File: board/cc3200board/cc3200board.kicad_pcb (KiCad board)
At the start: 4 copper layers, 40.4 x 30.8 mm, 44 parts, among them P1 PROG, P3 CONN_JTAG, U1 CC3200R1M2RGCR, U2 N25Q128A13ESE40E, X1 32.768kH, X2 ABM3B-40.000MHZ-10-1-U-T

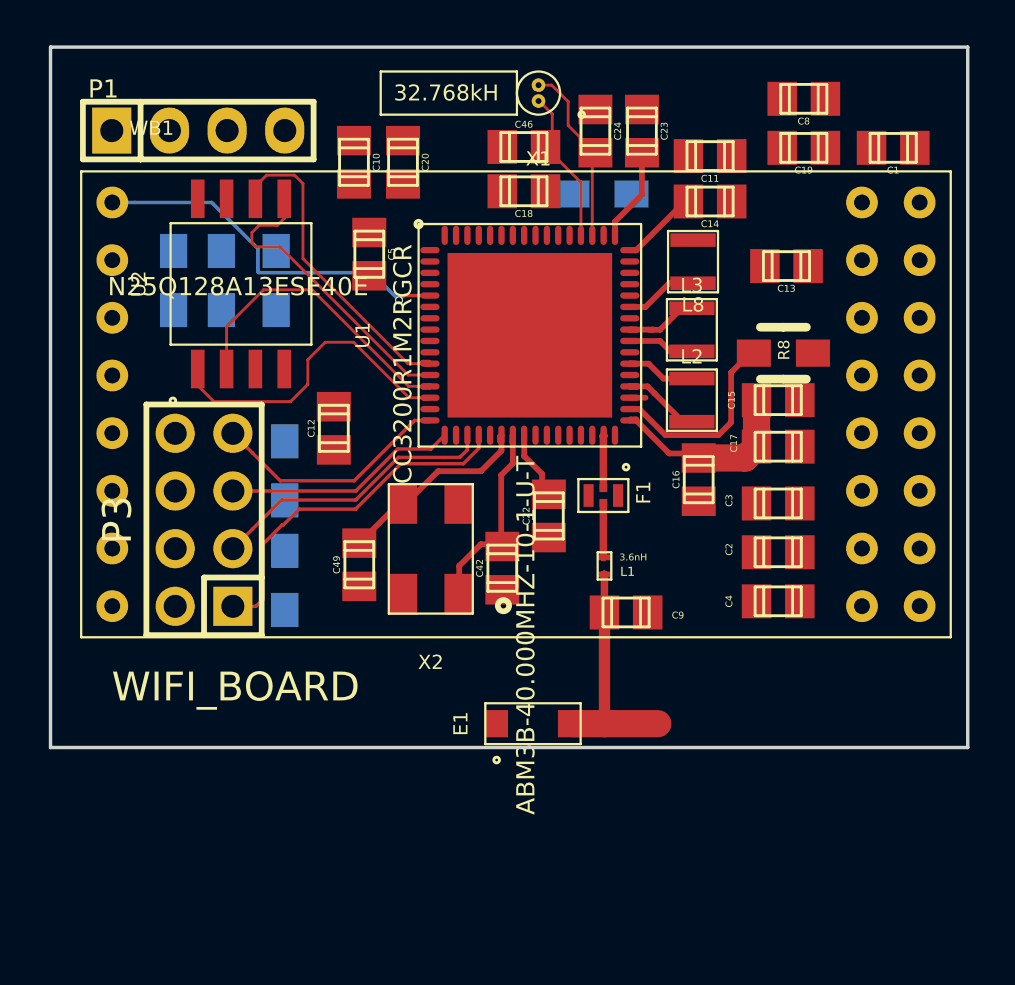
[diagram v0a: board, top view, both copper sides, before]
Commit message: Routed PA and DIG power planes
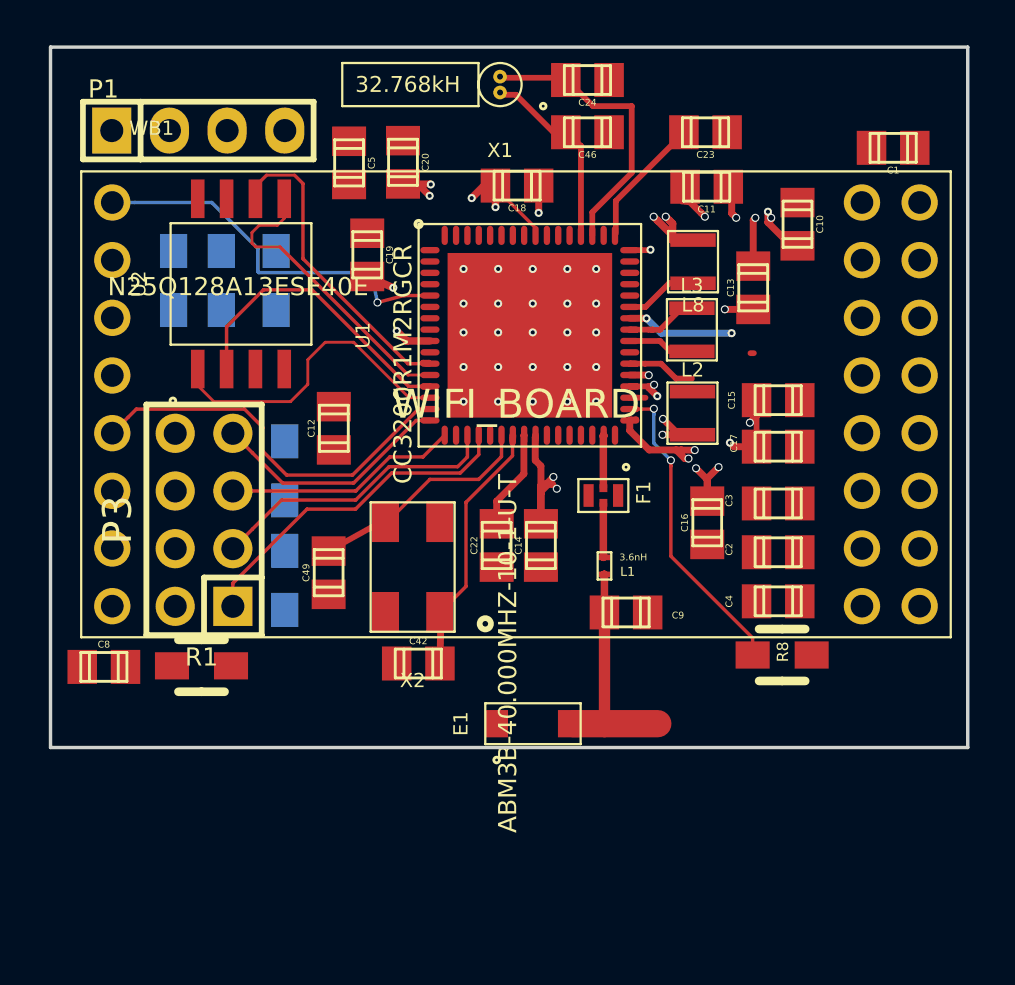
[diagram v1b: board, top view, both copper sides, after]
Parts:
- R1: moved to F.Cu
- moved C8 39.7 mm to (117.0, 155.4), turned to 0 degrees
- moved R1 27.3 mm to (121.3, 155.4)
- moved C19 19.8 mm to (128.6, 137.3), turned to 270 degrees
- moved C10 19.7 mm to (147.6, 135.9)
- moved C14 16.9 mm to (136.2, 150.1), turned to 90 degrees
- moved R8 13.3 mm to (146.9, 154.9)
- moved C42 5.60 mm to (130.8, 155.3), turned to 0 degrees
- moved C5 4.12 mm to (127.8, 133.2)
- moved C46 2.87 mm to (138.3, 131.9), turned to 180 degrees
- moved C23 2.80 mm to (143.5, 131.9), turned to 180 degrees
- moved C22 2.64 mm to (134.3, 150.1)
- moved C24 2.28 mm to (138.3, 129.6), turned to 180 degrees
- moved C16 1.94 mm to (143.6, 149.1)
- moved C13 1.75 mm to (145.6, 138.8), turned to 90 degrees
- moved X1 1.74 mm to (134.4, 129.8)
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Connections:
- net Net-(C10-Pad1) renamed /DCDC_ANA
- net Net-(C15-Pad1) renamed /DC_PA
- net Net-(C18-Pad1) renamed /DCDC_DIG
- U1 pad 26: (no net) -> Net-(U1-Pad26)
- U1 pad 27: (no net) -> Net-(U1-Pad27)
- U1 pad 28: (no net) -> Net-(U1-Pad28)
- U1 pad 29: (no net) -> Net-(U1-Pad29)
- U1 pad 30: (no net) -> Net-(U1-Pad30)
- U1 pad 46: (no net) -> Net-(U1-Pad46)
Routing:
- net GND: track 10.4 -> 68.9 mm, vias 0 -> 28
- net /cc3200-io/GPIO22: track 0.00 -> 17.5 mm
- net /DCDC_DIG: track 0.00 -> 15.0 mm, vias 0 -> 8
- net /DCDC_ANA: track 7.93 -> 21.0 mm, vias 0 -> 11
- net /DC_PA: track 12.4 -> 19.0 mm, vias 0 -> 8
- net Net-(R8-Pad1): track 8.72 -> 13.7 mm, vias 0 -> 2
- net Net-(C24-Pad1): track 8.13 -> 12.9 mm
- net Net-(C42-Pad1): track 9.69 -> 12.1 mm
- net Net-(C22-Pad1): track 3.25 -> 5.36 mm
- net Net-(C23-Pad1): track 5.02 -> 6.11 mm
- net /cc3200-io/GPIO12: track 0.00 -> 1.04 mm
- net Net-(C49-Pad1): track 10.1 -> 11.0 mm
- net 3V3: track 0.00 -> 0.84 mm, vias 0 -> 1
- net /cc3200-io/TMS: track 15.9 -> 15.3 mm
- net /cc3200-io/GPIO14: track 16.5 -> 17.0 mm
- added copper zone on In2.Cu, net /DCDC_ANA
- added copper zone on In2.Cu, net /DCDC_DIG
- added copper zone on In2.Cu, net /DC_PA
- added copper zone on In2.Cu, net 3V3
- added copper zone on B.Cu, net GND
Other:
- net class 50OHM: clearance 0.381 -> 0.127

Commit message: Completed power reroute, PCB plane cleanup. Two DRC violations on DCDC_DIG and DCDC_ANA intersection left.
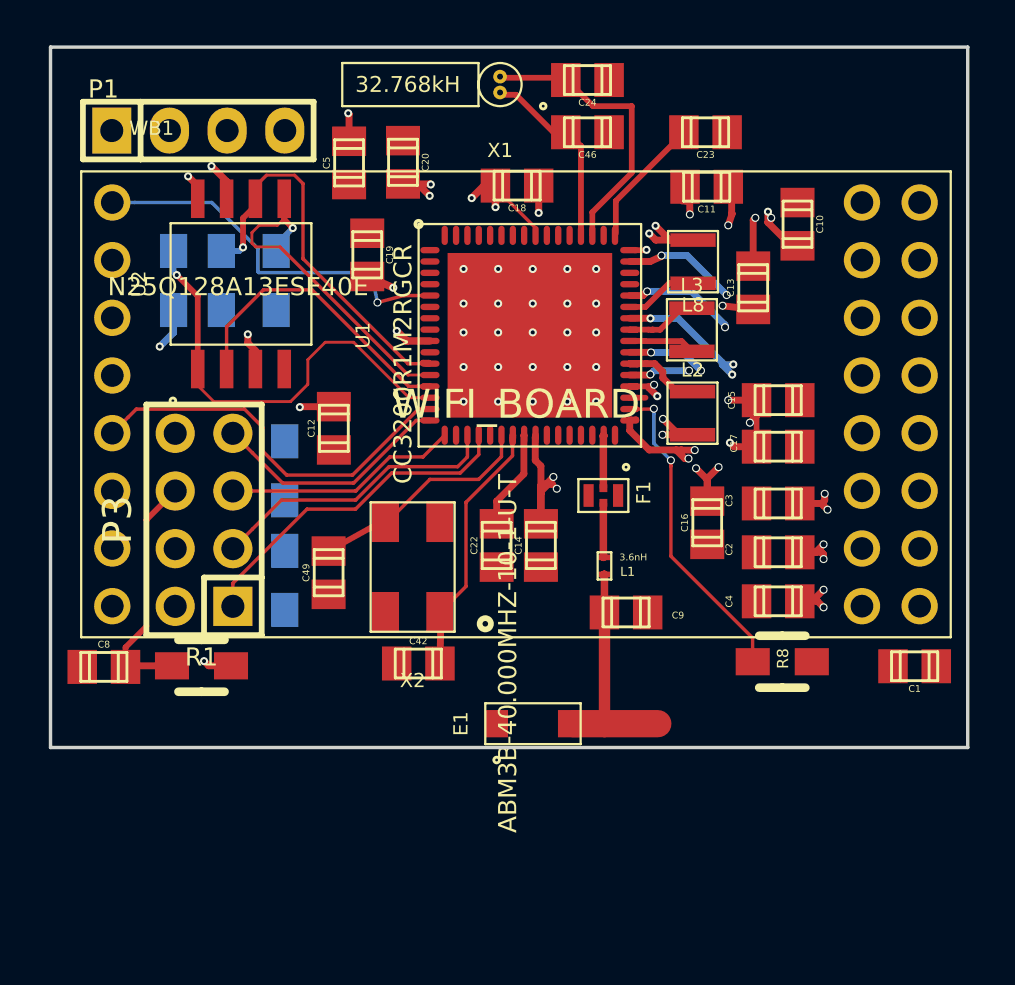
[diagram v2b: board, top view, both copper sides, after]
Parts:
- moved C1 22.9 mm to (152.7, 155.4)
- moved R8 0.30 mm to (146.9, 155.2)
- turned C5 to 90 degrees
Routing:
- net 3V3: track 0.84 -> 33.5 mm, vias 1 -> 21
- net /cc3200-io/nRESET: track 0.00 -> 12.4 mm
- net Net-(R2-Pad2): track 14.6 -> 21.3 mm, vias 0 -> 1
- net Net-(R3-Pad2): track 16.1 -> 20.3 mm, vias 0 -> 1
- net Net-(R4-Pad2): track 16.5 -> 20.6 mm, vias 0 -> 1
- net /DC_PA: track 19.0 -> 21.6 mm, vias 8 -> 10
- net Net-(L2-Pad2): track 4.06 -> 5.21 mm
- net /DCDC_ANA: track 21.0 -> 20.5 mm
- added copper zone on In2.Cu, net GND

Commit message: Finished major layout, RF vias and final ground pins left
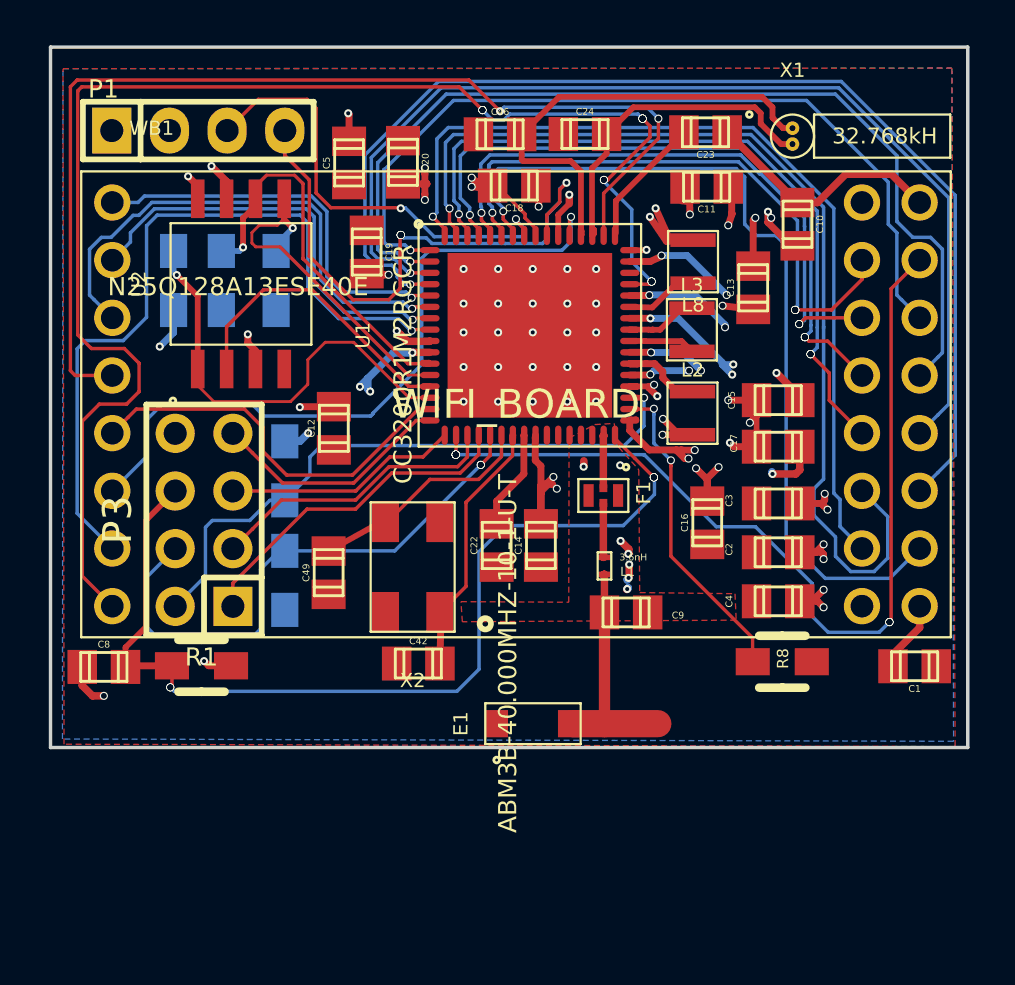
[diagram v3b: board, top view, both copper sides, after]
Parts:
- moved X1 13.1 mm to (147.3, 132.1), turned to 0 degrees
- moved C46 3.85 mm to (134.4, 132.0), turned to 0 degrees
- moved C24 2.38 mm to (138.2, 132.0), turned to 0 degrees
- moved C19 0.13 mm to (128.6, 137.2)
- moved C18 0.12 mm to (135.1, 134.2)
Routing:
- net /cc3200-io/GPIO31: track 0.00 -> 63.0 mm, vias 0 -> 12
- net /cc3200-io/GPIO13: track 0.00 -> 51.0 mm, vias 0 -> 1
- net /cc3200-io/GPIO0: track 0.00 -> 47.4 mm, vias 0 -> 2
- net /cc3200-io/GPIO12: track 1.04 -> 47.8 mm, vias 0 -> 1
- net /cc3200-io/GPIO8: track 0.00 -> 44.7 mm, vias 0 -> 1
- net /cc3200-io/GPIO11: track 0.00 -> 43.0 mm, vias 0 -> 1
- net /cc3200-io/GPIO28: track 0.00 -> 40.7 mm, vias 0 -> 11
- net /cc3200-io/GPIO9: track 0.00 -> 39.2 mm, vias 0 -> 1
- net /cc3200-io/GPIO3: track 0.00 -> 38.7 mm, vias 0 -> 1
- net /cc3200-io/GPIO10: track 0.00 -> 36.9 mm, vias 0 -> 1
- net /cc3200-io/GPIO17: track 0.00 -> 33.6 mm, vias 0 -> 1
- net /cc3200-io/nRESET: track 12.4 -> 45.2 mm, vias 0 -> 6
- net /cc3200-io/GPIO7: track 0.00 -> 32.3 mm, vias 0 -> 4
- net /cc3200-io/GPIO30: track 0.00 -> 30.8 mm, vias 0 -> 1
- net /cc3200-io/GPIO6: track 0.00 -> 29.3 mm, vias 0 -> 4
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- added copper zone on F.Cu, net GND

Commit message: Rev 1.0 of CC3200board
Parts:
- turned C9 to 180 degrees
- turned E1 to 270 degrees
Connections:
- C9 pad 1: GND -> /FEED
- E1 pad 1: GND -> /FEED
- L1 pad 2: GND -> /FEED
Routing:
- net GND: track 89.5 -> 143.7 mm, vias 39 -> 84
- net /FEED: track 0.00 -> 6.69 mm
- net 3V3: track 50.1 -> 53.1 mm
- net (no net): track 0.00 -> 1.97 mm
- net /cc3200-io/SOP0: track 28.3 -> 27.1 mm
- net /cc3200-io/GPIO14: track 17.7 -> 16.5 mm
- net /cc3200-io/nRESET: track 45.2 -> 45.9 mm
- net Net-(C46-Pad1): track 21.4 -> 22.0 mm
- net Net-(R8-Pad1): track 13.7 -> 14.3 mm
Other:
- net class 50OHM: clearance 0.127 -> 0
- net class FEED added: clearance 0, trace_width 0.5, via_dia 0.3556, via_drill 0.254

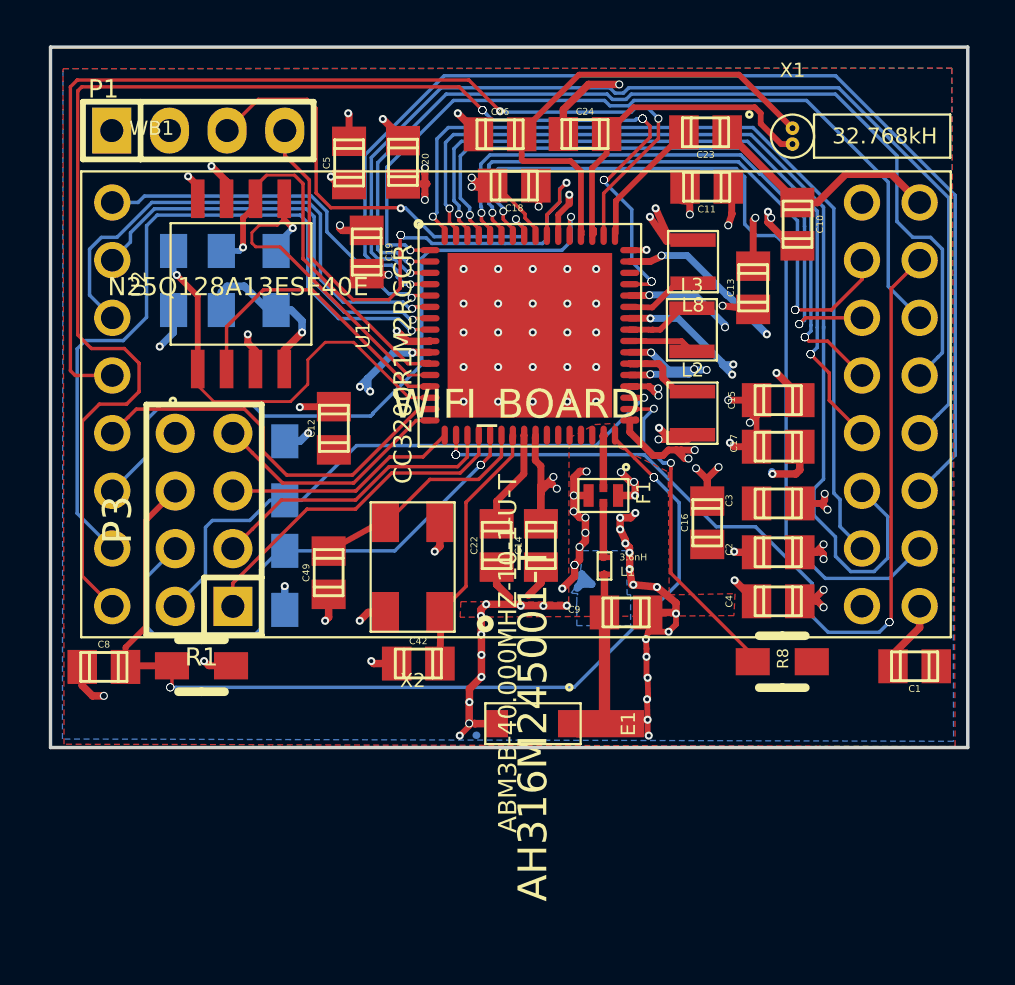
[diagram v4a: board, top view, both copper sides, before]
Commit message: Fixed error in GND plane on L4
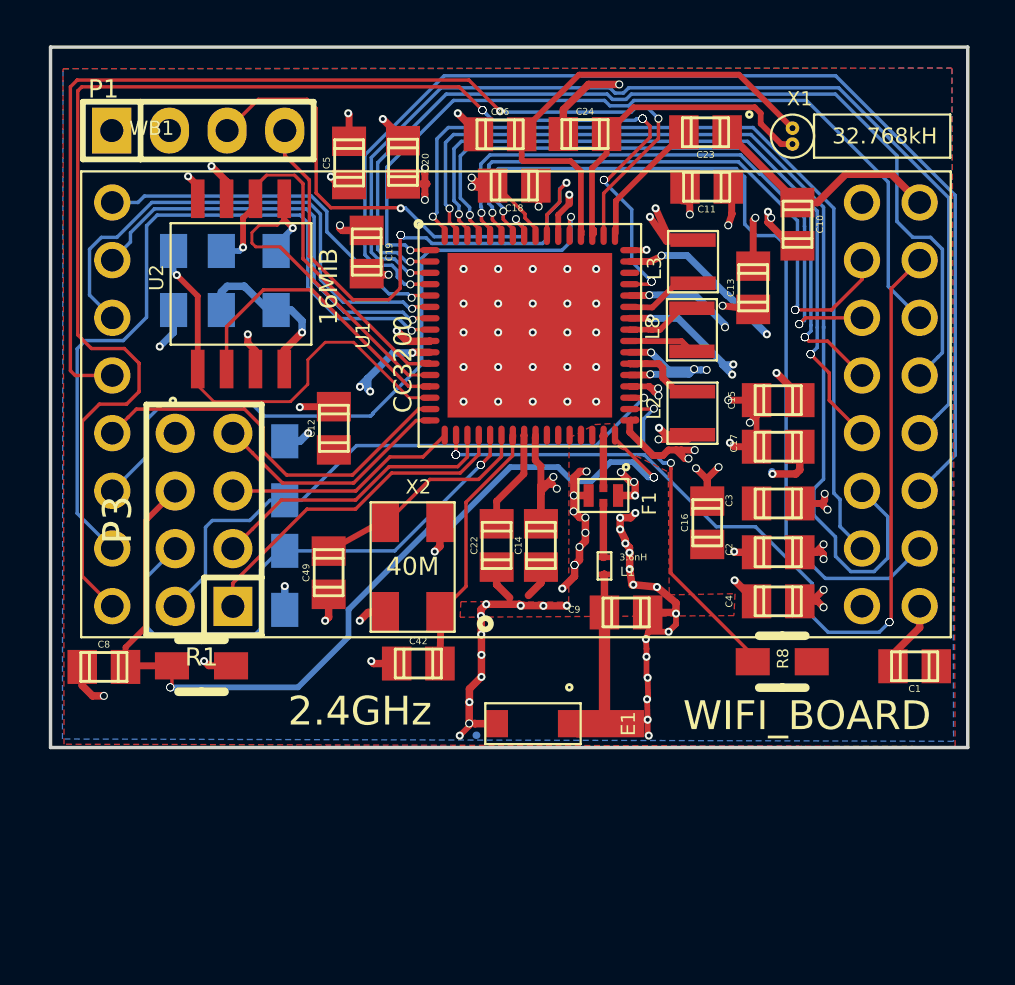
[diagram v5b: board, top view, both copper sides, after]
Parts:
- E1: value AH316M245001-T -> 2.4GHz
- U1: value CC3200R1M2RGCR -> CC3200
- U2: value N25Q128A13ESE40E -> 16MiB
- X2: value ABM3B-40.000MHZ-10-1-U-T -> 40M
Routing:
- net /cc3200-io/nRESET: track 45.9 -> 43.7 mm
- net (no net): track 1.97 -> 0.02 mm

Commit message: Revision 1.1 commit. Version submitted to OSH
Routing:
- net GND: track 143.7 -> 144.9 mm
- net /FEED: track 6.69 -> 7.30 mm
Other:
- board text added: "Hasith V, Darren S Robert N."
- board text added: "r1.1"
